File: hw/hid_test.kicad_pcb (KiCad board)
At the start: 2 copper layers, 125 parts, among them J1 USB_B_Micro, J10 TWI, J2 2x8 Connector, J3 ISP, J4 2x8 Connector, J5 2x8, J6 ILI9163, J7 ILI9163, J8 ILI9163, J9 ILI9163, Q1 2N3904, SW1 SW_Push, SW10 Btn, SW11 Btn, SW12 Btn, SW13 Btn, SW14 Btn, SW15 Btn, SW16 Btn, SW17 Btn, SW18 Btn, SW19 Btn, SW2 Btn, SW20 Btn, SW21 Btn, SW22 Btn, SW23 Btn, SW24 Btn, SW25 Btn, SW26 Btn, SW27 Btn, SW28 Btn, SW29 Btn, SW3 Btn, SW30 Btn, SW31 Btn, SW32 Btn, SW33 Btn, SW34 Btn, SW35 Btn, SW36 Btn, SW37 Btn, SW38 Btn, SW39 Btn, SW4 Btn, SW40 Btn, SW41 Btn, SW5 Btn, SW6 Btn, SW7 Btn, SW8 Btn, SW9 Btn, U1 ATmega644-20PU, U2 CD4555BE, U3 LD1117S33TR, Y1 20MHz

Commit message: PCB component placing before routing
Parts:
- U3: footprint Package_TO_SOT_THT:TO-220-3_Vertical -> Package_TO_SOT_THT:TO-220-3_Horizontal_TabDown
- moved SW27 251.5 mm to (35.6, 31.1)
- moved SW22 249.1 mm to (24.1, 17.8)
- moved SW25 245.1 mm to (24.1, 57.8)
- moved SW31 238.3 mm to (47.0, 31.1)
- moved SW26 236.1 mm to (35.6, 17.8)
- moved D27 234.9 mm to (31.8, 66.0), turned to 180 degrees
- moved D26 233.0 mm to (31.8, 52.1), turned to 180 degrees
- moved SW29 231.6 mm to (35.6, 57.8)
- moved SW33 230.8 mm to (47.0, 57.8)
- moved SW24 228.8 mm to (24.1, 44.5)
- moved SW37 227.6 mm to (58.3, 57.8)
- moved SW36 226.2 mm to (58.4, 44.5)
- moved SW30 223.3 mm to (47.0, 17.8)
- moved SW34 222.4 mm to (58.4, 17.8)
- moved SW32 214.8 mm to (47.0, 44.5)
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
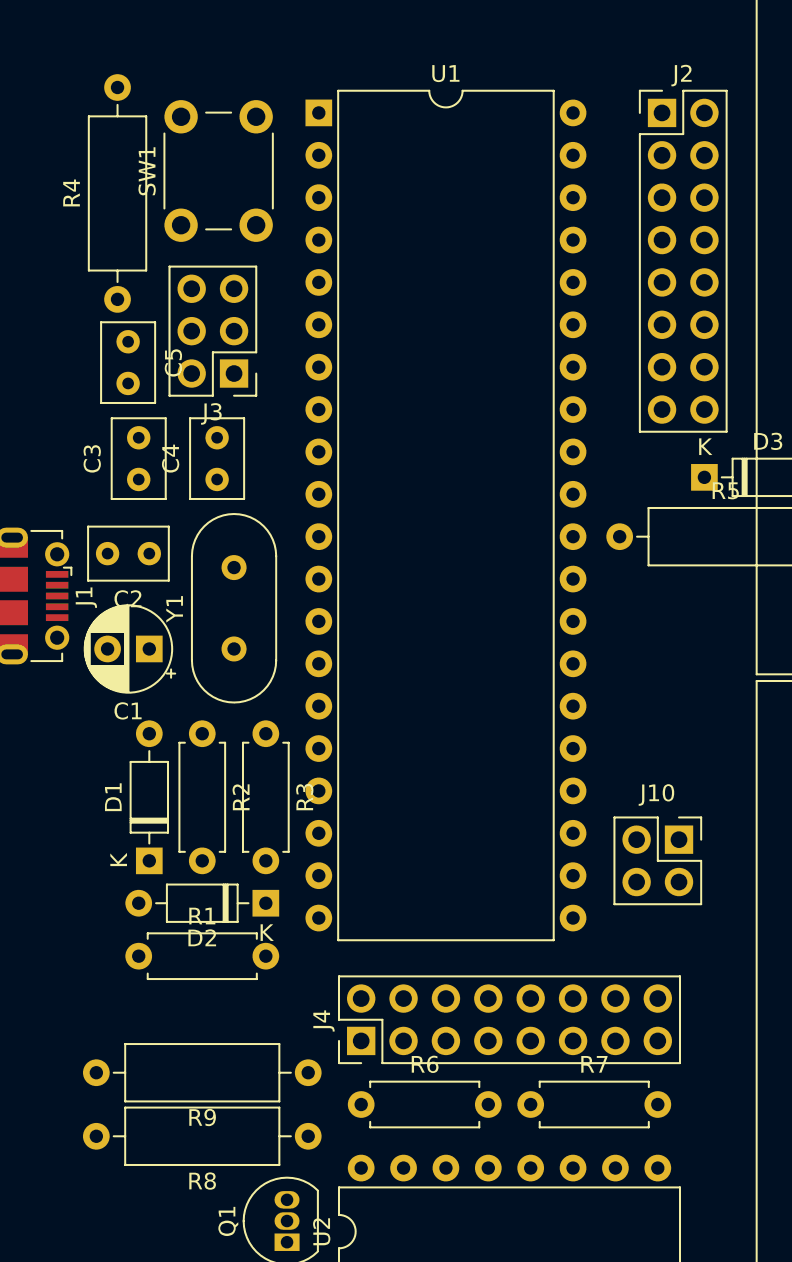
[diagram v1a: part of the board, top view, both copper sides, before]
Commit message: Little adjustments and basic design limits
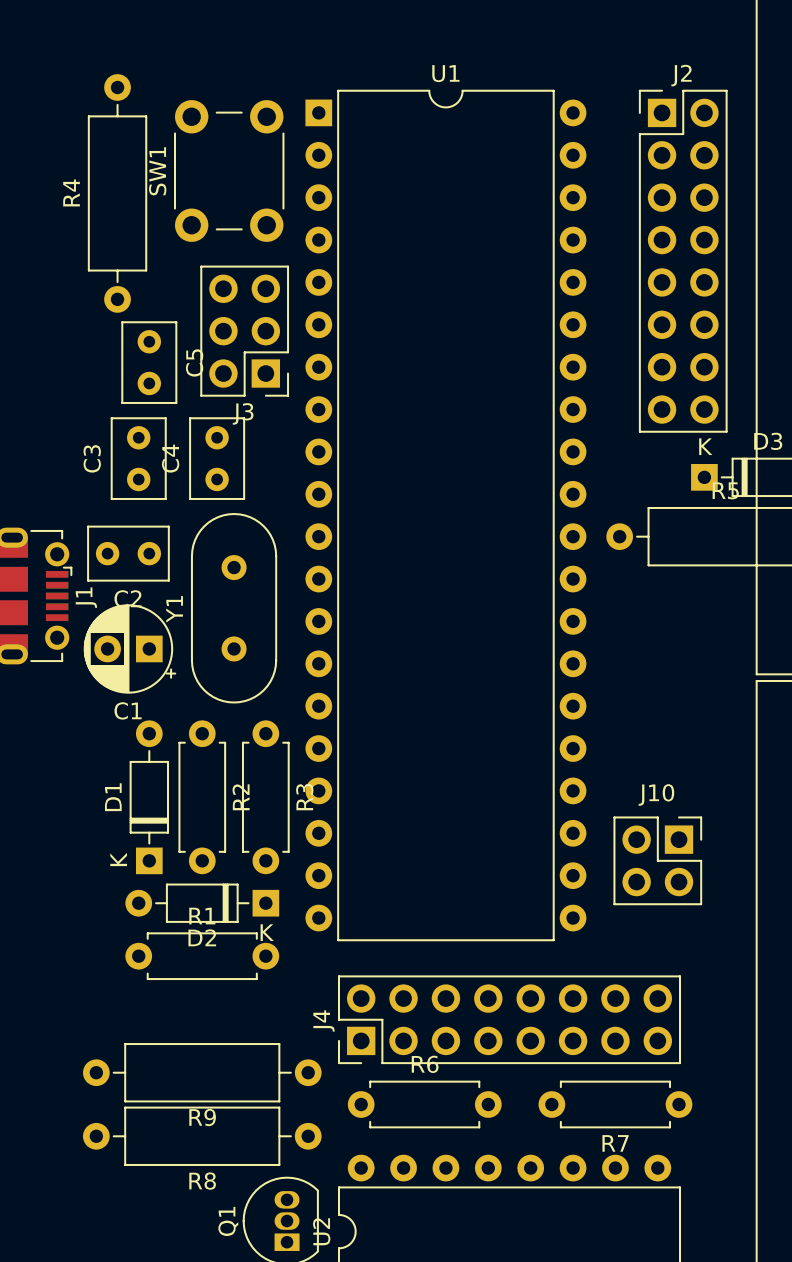
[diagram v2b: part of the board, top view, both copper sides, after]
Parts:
- moved R7 8.89 mm to (90.2, 162.6), turned to 180 degrees
- moved J3 1.91 mm to (65.4, 118.7)
- moved C5 1.27 mm to (58.4, 116.8)
- moved SW1 0.63 mm to (61.0, 109.9)
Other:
- net class Default: trace_width 0.25 -> 0.2; via_dia 0.8 -> 0.4; via_drill 0.4 -> 0.3
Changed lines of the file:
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@@
   )
   (setup
-    (last_trace_width 0.25)
+    (last_trace_width 0.4)
+    (user_trace_width 0.3)
+    (user_trace_width 0.4)
+    (user_trace_width 0.8)
+    (user_trace_width 1.6)
+    (user_trace_width 3.2)
     (trace_clearance 0.2)
     (zone_clearance 0.508)
     (zone_45_only no)
     (trace_min 0.2)
-    (via_size 0.8)
-    (via_drill 0.4)
+    (via_size 0.4)
+    (via_drill 0.3)
     (via_min_size 0.4)
     (via_min_drill 0.3)
@@
   (net_class Default "This is the default net class."
     (clearance 0.2)
-    (trace_width 0.25)
-    (via_dia 0.8)
-    (via_drill 0.4)
+    (trace_width 0.2)
+    (via_dia 0.4)
+    (via_drill 0.3)
     (uvia_dia 0.3)
     (uvia_drill 0.1)
@@
   )
   (module Button_Switch_THT:SW_PUSH_6mm (layer F.Cu)
-    (at 60.325 109.855 90)
+    (at 60.96 109.855 90)
     (descr https://www.omron.com/ecb/products/pdf/en-b3f.pdf)
     (tags "tact sw push 6mm")
@@
   )
   (module Resistor_THT:R_Axial_DIN0207_L6.3mm_D2.5mm_P7.62mm_Horizontal (layer F.Cu)
-    (at 81.28 162.56)
+    (at 90.17 162.56 180)
     (descr "Resistor, Axial_DIN0207 series, Axial, Horizontal, pin pitch=7.62mm, 0.25W = 1/4W, length*diameter=6.3*2.5mm^2, http://cdn-reichelt.de/documents/datenblatt/B400/1_4W%23YAG.pdf")
     (tags "Resistor Axial_DIN0207 series Axial Horizontal pin pitch 7.62mm 0.25W = 1/4W length 6.3mm diameter 2.5mm")
@@
     (fp_line (start 0.66 1.25) (end 6.96 1.25) (layer F.Fab) (width 0.1))
     (fp_line (start 0.66 -1.25) (end 0.66 1.25) (layer F.Fab) (width 0.1))
-    (pad 2 thru_hole oval (at 7.62 0) (size 1.6 1.6) (drill 0.8) (layers *.Cu *.Mask)
+    (pad 2 thru_hole oval (at 7.62 0 180) (size 1.6 1.6) (drill 0.8) (layers *.Cu *.Mask)
       (net 88 TWI_SCL))
-    (pad 1 thru_hole circle (at 0 0) (size 1.6 1.6) (drill 0.8) (layers *.Cu *.Mask)
+    (pad 1 thru_hole circle (at 0 0 180) (size 1.6 1.6) (drill 0.8) (layers *.Cu *.Mask)
       (net 75 +5V))
     (model ${KISYS3DMOD}/Resistor_THT.3dshapes/R_Axial_DIN0207_L6.3mm_D2.5mm_P7.62mm_Horizontal.wrl
@@
   )
   (module Capacitor_THT:C_Rect_L4.6mm_W3.0mm_P2.50mm_MKS02_FKP02 (layer F.Cu)
-    (at 57.15 116.84 270)
+    (at 58.42 116.84 270)
     (descr "C, Rect series, Radial, pin pitch=2.50mm, , length*width=4.6*3.0mm^2, Capacitor, http://www.wima.de/DE/WIMA_MKS_02.pdf")
     (tags "C Rect series Radial pin pitch 2.50mm  length 4.6mm width 3.0mm Capacitor")
@@
   )
   (module Connector_PinHeader_2.54mm:PinHeader_2x03_P2.54mm_Vertical (layer F.Cu)
-    (at 63.5 118.745 180)
+    (at 65.405 118.745 180)
     (descr "Through hole straight pin header, 2x03, 2.54mm pitch, double rows")
     (tags "Through hole pin header THT 2x03 2.54mm double row")

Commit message: Can't have too many vias, right?
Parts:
- moved D20 146.1 mm to (16.8, 110.9), turned to 0 degrees
- moved J7 144.6 mm to (183.6, 43.8), turned to 180 degrees
- moved SW18 144.2 mm to (24.4, 118.5), turned to 180 degrees
- moved J6 133.4 mm to (183.6, 73.8), turned to 180 degrees
- moved D21 132.3 mm to (16.8, 97.5), turned to 0 degrees
- moved SW14 128.9 mm to (35.8, 118.5), turned to 180 degrees
- moved D16 128.3 mm to (28.2, 110.9), turned to 0 degrees
- moved SW19 127.1 mm to (24.4, 105.2), turned to 180 degrees
- moved U2 125.2 mm to (174.6, 103.5), turned to 180 degrees
- moved Q1 124.4 mm to (174.0, 108.0), turned to 0 degrees
- moved D22 122.8 mm to (16.8, 84.2), turned to 0 degrees
- moved R6 120.4 mm to (157.7, 79.0), turned to 270 degrees
- moved D23 119.3 mm to (16.8, 70.9), turned to 0 degrees
- moved RN2 118.5 mm to (162.6, 43.2), turned to 180 degrees
- moved SW10 116.0 mm to (47.2, 118.5), turned to 180 degrees
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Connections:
- J7 pad 7: Net-(J7-Pad7) -> SPI_SCK_3v3
- J8 pad 7: Net-(J7-Pad7) -> SPI_SCK_3v3
- J9 pad 7: Net-(J7-Pad7) -> SPI_SCK_3v3
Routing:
- net +3V3: track 0.00 -> 239.3 mm
- net SPI_SDA_3v3: track 0.00 -> 211.1 mm, vias 0 -> 4
- net +5V: track 0.00 -> 171.2 mm
- net DISPLAY_~RST~_3v3: track 0.00 -> 166.9 mm, vias 0 -> 3
- net Switch_Matrix_E: track 0.00 -> 163.3 mm
- net SPI_SCK_3v3: track 0.00 -> 161.5 mm, vias 0 -> 4
- net SPI_~SS~_3v3: track 0.00 -> 161.3 mm, vias 0 -> 6
- net Switch_Matrix_D: track 0.00 -> 157.7 mm
- net Switch_Matrix_C: track 0.00 -> 145.4 mm
- net Switch_Matrix_B: track 0.00 -> 130.5 mm
- net Switch_Matrix_A: track 0.00 -> 117.3 mm
- net MatrixBoard_Row_1: track 0.00 -> 96.6 mm
- net Matrix_2b: track 0.00 -> 95.8 mm
- net MatrixBoard_Row_2: track 0.00 -> 89.8 mm
- net Matrix_0b: track 0.00 -> 89.7 mm
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- added copper zone on F.Cu, net (none)
- added copper zone on B.Cu, net GND
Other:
- board outline added: 175.3 x 111.5 mm

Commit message: Little fixes
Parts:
- D10, D11, D12, D13, D14, D15, D16, D17, D18, D19, D20, D21, D22, D23, D24, D25, D26, D27, D28, D29, D30, D31, D32, D33, D34, D35, D36, D37, D38, D39, D4, D40, D41, D42, D43, D5, D6, D7, D8, D9: footprint Diode_THT:D_DO-35_SOD27_P7.62mm_Horizontal -> hw:D_DO-35_SOD27_P7.62mm_Horizontal_No_Ref
- moved D20 4.58 mm to (20.6, 113.4)
- moved D22 4.58 mm to (20.6, 86.7)
- moved D23 4.58 mm to (20.6, 73.4)
- moved D40 4.58 mm to (20.6, 60.1)
- moved D16 4.58 mm to (32.0, 113.4)
- moved D18 4.58 mm to (32.0, 86.7)
- moved D19 4.58 mm to (32.0, 73.4)
- moved D38 4.58 mm to (32.0, 33.4)
- moved D39 4.58 mm to (32.0, 19.4)
- moved D42 4.58 mm to (19.9, 33.4)
- moved D43 4.58 mm to (19.9, 19.4)
- moved D10 4.58 mm to (54.9, 86.7)
- moved D11 4.58 mm to (54.9, 73.4)
- moved D12 4.58 mm to (43.4, 113.4)
- moved D14 4.58 mm to (43.4, 86.7)
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- renumbered SW2 to SW_1, SW19 to SW_10, SW4 to SW_11, SW8 to SW_12, SW12 to SW_13, SW16 to SW_14, SW20 to SW_15, SW5 to SW_16, SW9 to SW_17, SW13 to SW_18, SW17 to SW_19, SW6 to SW_2, SW21 to SW_20, SW22 to SW_21, SW26 to SW_22, SW30 to SW_23, SW34 to SW_24, SW38 to SW_25, SW23 to SW_26, SW27 to SW_27, SW31 to SW_28, SW35 to SW_29, SW10 to SW_3, SW39 to SW_30, SW24 to SW_31, SW28 to SW_32, SW32 to SW_33, SW36 to SW_34, SW40 to SW_35, SW25 to SW_36, SW29 to SW_37, SW33 to SW_38, SW37 to SW_39, SW14 to SW_4, SW41 to SW_40, SW18 to SW_5, SW3 to SW_6, SW7 to SW_7, SW11 to SW_8, SW15 to SW_9

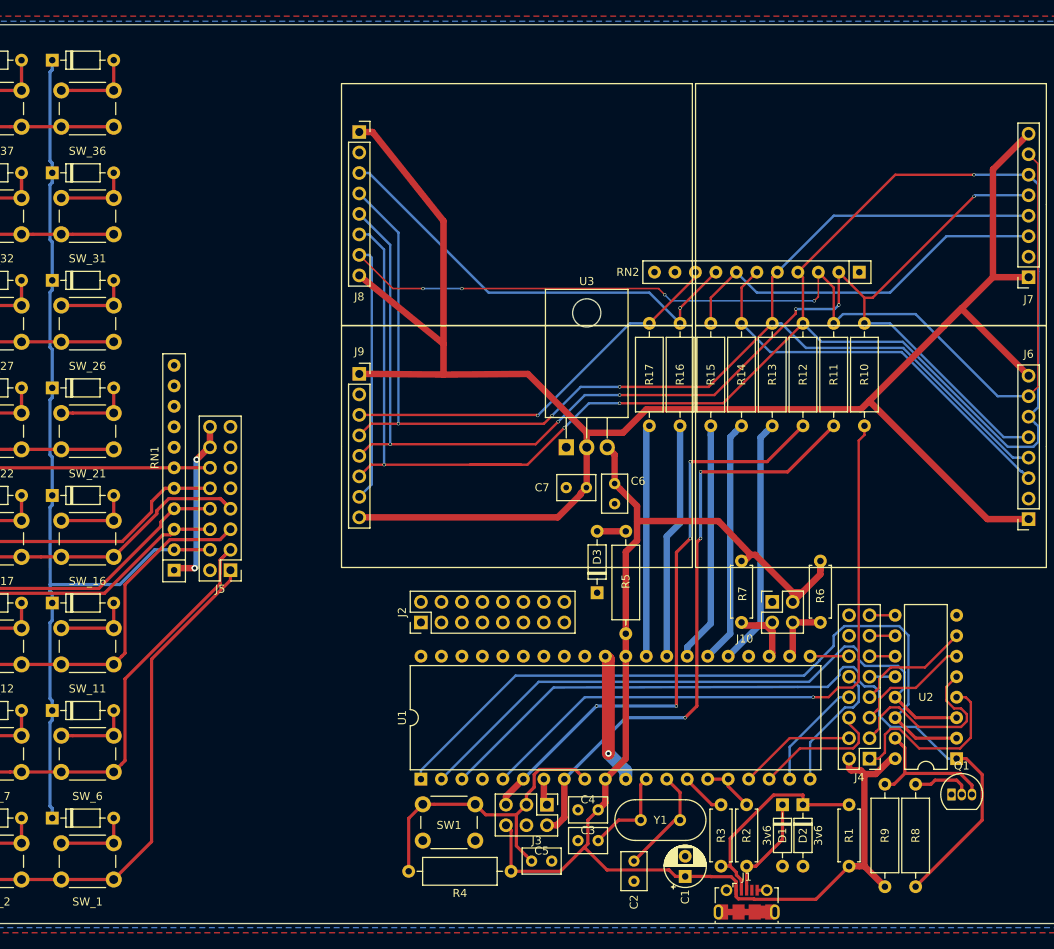
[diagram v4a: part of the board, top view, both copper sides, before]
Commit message: Fix GND in couple places. Added drill files
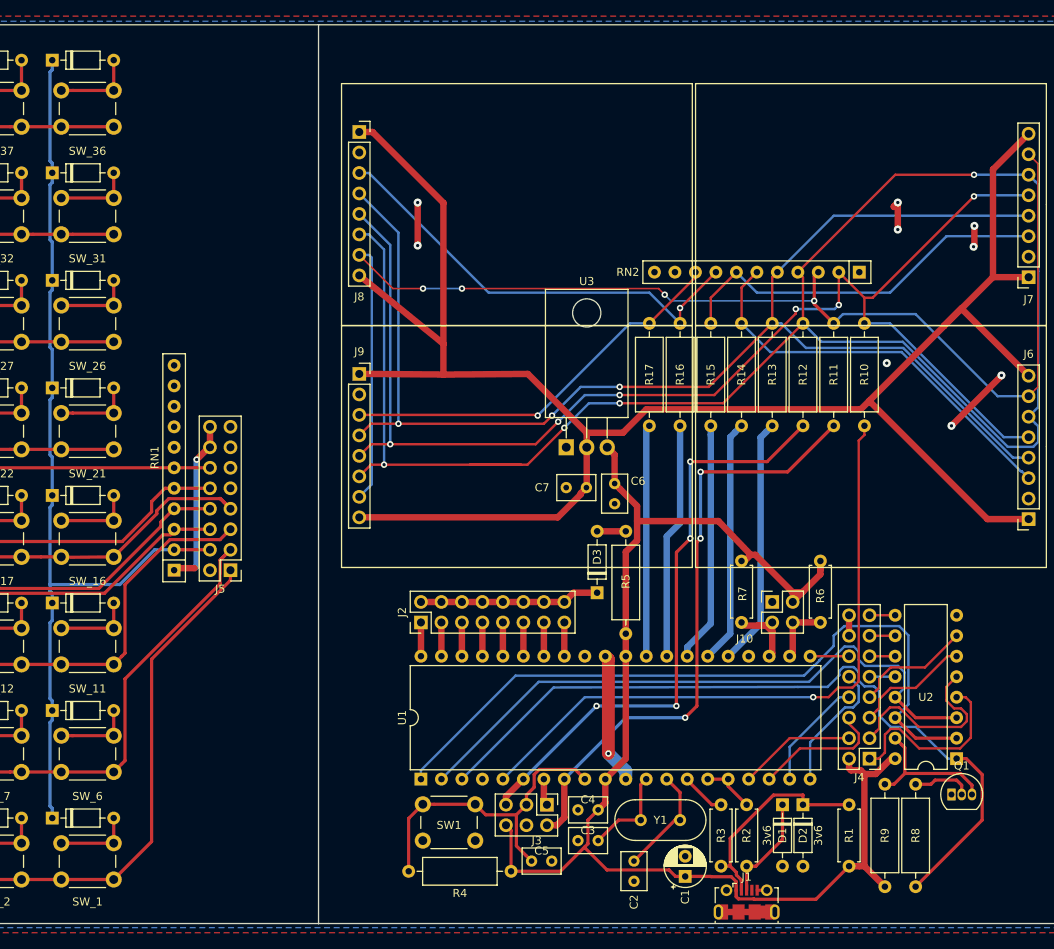
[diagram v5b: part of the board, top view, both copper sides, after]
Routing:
- net GND: track 44.8 -> 68.3 mm, vias 3 -> 10
- net Net-(D3-Pad1): track 0.00 -> 22.3 mm
- net Net-(J2-Pad9): track 0.00 -> 4.19 mm
- net Net-(J2-Pad7): track 0.00 -> 4.19 mm
- net Net-(J2-Pad5): track 0.00 -> 4.19 mm
- net Net-(J2-Pad3): track 0.00 -> 4.19 mm
- net Net-(J2-Pad15): track 0.00 -> 4.19 mm
- net Net-(J2-Pad13): track 0.00 -> 4.19 mm
- net Net-(J2-Pad11): track 0.00 -> 4.19 mm
- net Net-(J2-Pad1): track 0.00 -> 4.19 mm
- net SPI_SCK_3v3: track 161.5 -> 158.1 mm
- net MatrixBoard_Row_4: track 72.3 -> 71.1 mm
- net +3V3: track 239.3 -> 239.8 mm
- net (no net): track 0.00 -> 0.05 mm, vias 0 -> 1
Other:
- outline, holes or cut-outs redrawn
- net class Default: via_dia 0.4 -> 0.8; via_drill 0.3 -> 0.4
